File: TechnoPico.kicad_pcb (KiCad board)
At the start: 2 copper layers, 138.3 x 70.6 mm, 160 parts, among them J1 USB_C_Receptacle_USB2.0, J2 Conn_01x02, SW1 Test, SW2 Service, SW3 BOOTSEL, U1 RP2350_60QFN, U2 SN74LV1T34DBV, U3 XC6206PxxxMR, U4 USBLC6-2SC6, Y1 12.000MHz

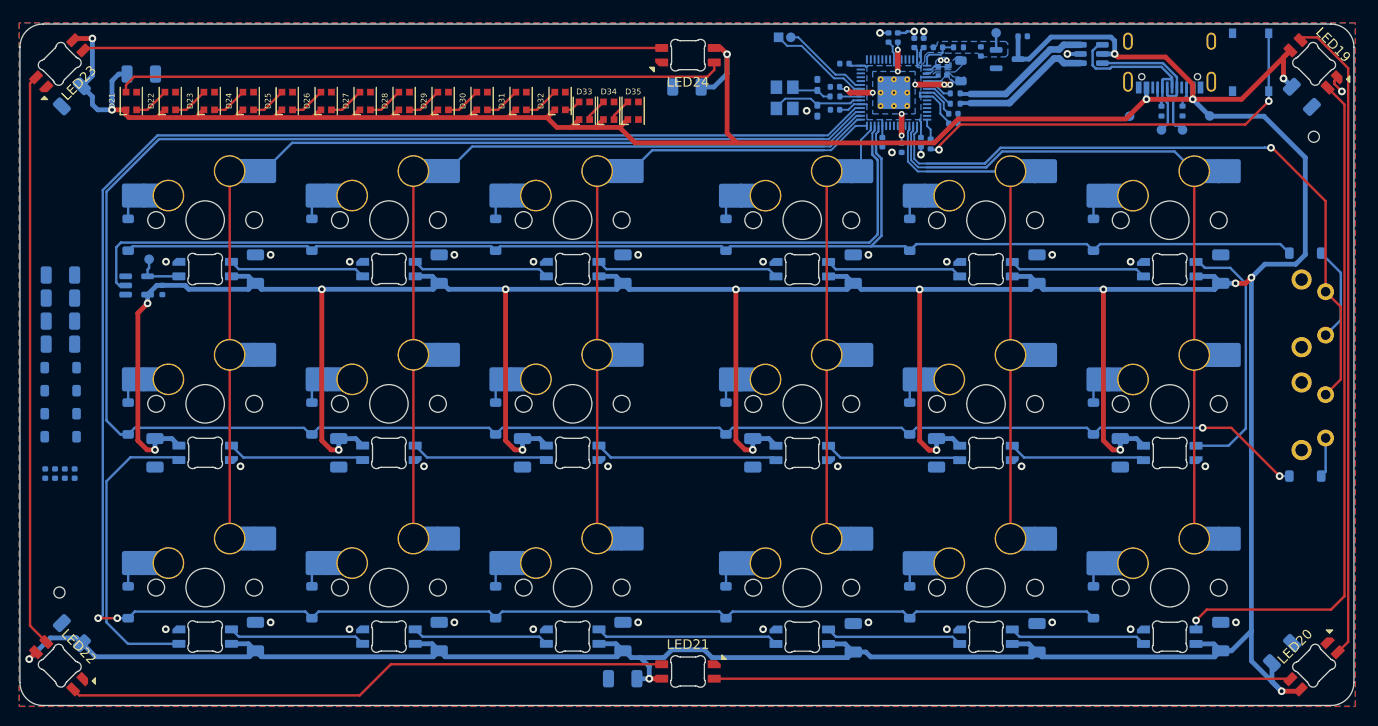
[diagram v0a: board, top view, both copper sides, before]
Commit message: Experimental corner cutouts for mounting
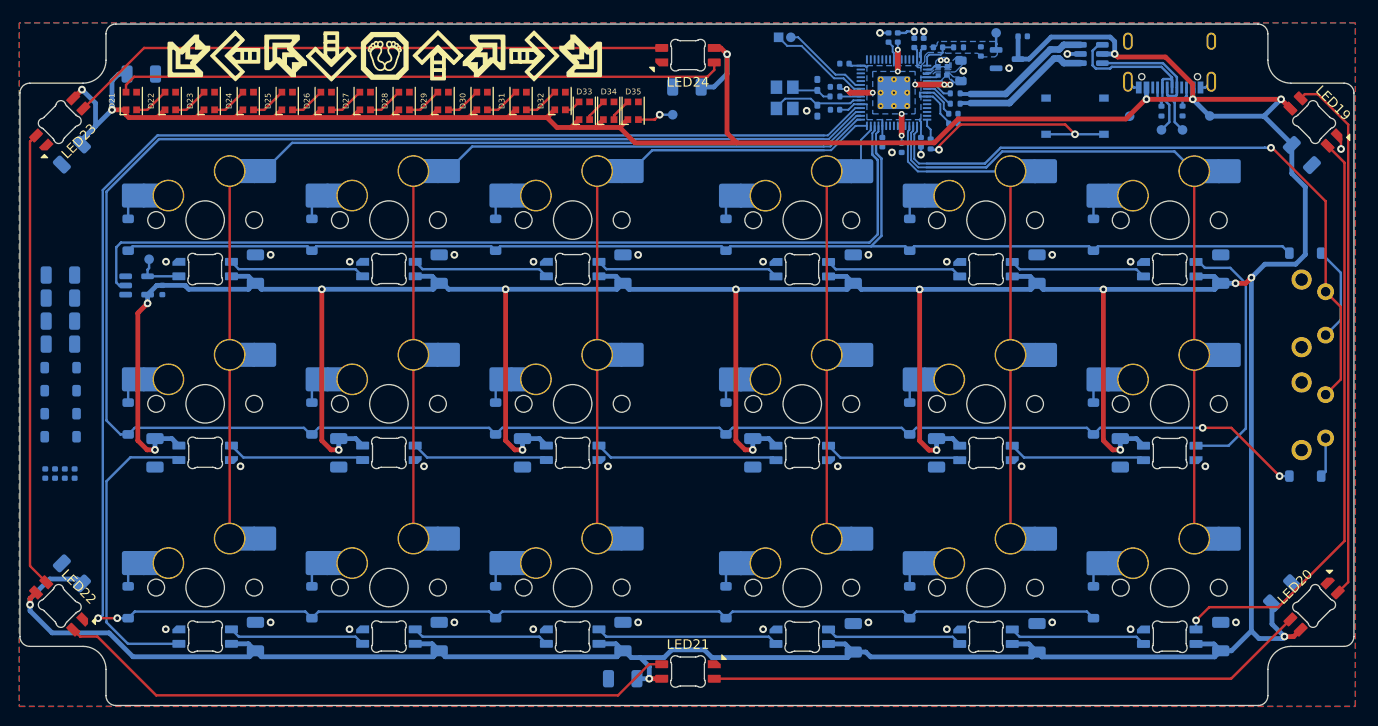
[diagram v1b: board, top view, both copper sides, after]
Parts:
- removed REF** (x2): MountingHole_ToolingHole_1.152mm, MountingHole:MountingHole_ToolingHole_1.152mm
- added TP7: EXT LED, TestPoint:TestPoint_Pad_D1.0mm, B.Cu at (135.2, 60.2)
- moved SW3 19.1 mm to (176.9, 60.4), turned to 0 degrees
- moved C41 6.19 mm to (198.4, 109.8)
- moved LED20 6.19 mm to (201.7, 111.1)
- moved C43 6.19 mm to (72.9, 107.8)
- moved LED22 6.19 mm to (71.7, 111.1)
- moved C40 6.03 mm to (200.4, 64.4)
- moved LED19 6.03 mm to (201.7, 61.0)
- moved C44 6.03 mm to (72.9, 64.3)
- moved LED23 6.03 mm to (71.7, 61.0)
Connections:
- D35 pad 2: unconnected-(D35-DOUT-Pad2) -> LED_EXT
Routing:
- net /BOOTSEL: track 44.4 -> 22.7 mm
- net Net-(LED22-DOUT): track 59.5 -> 47.3 mm
- net Net-(LED19-DOUT): track 67.4 -> 55.4 mm
- net LED_ZONE2: track 70.8 -> 61.4 mm
- net LED_EXT: track 0.00 -> 3.76 mm, vias 0 -> 1
- net Net-(LED21-DOUT): track 62.6 -> 65.2 mm
- net Net-(LED20-DOUT): track 59.8 -> 62.3 mm
- net Net-(LED23-DOUT): track 60.1 -> 62.6 mm
- net GND: track 9.48 -> 11.8 mm, vias 39 -> 41
- net +5V: track 714.0 -> 716.1 mm
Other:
- outline, holes or cut-outs redrawn
- board text added: "DESIGNED BY DJ505 2024"
- board text added: "DOUT"
- board text added: "https://github.com/dj505/TechnoPico"

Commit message: Revert main PCB corner cutouts, add holes to plate
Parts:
- added REF**: MountingHole_ToolingHole_1.152mm, MountingHole:MountingHole_ToolingHole_1.152mm, F.Cu at (71.6, 109.7)
- added REF**: MountingHole_ToolingHole_1.152mm, MountingHole:MountingHole_ToolingHole_1.152mm, F.Cu at (201.7, 62.5)
- moved C41 6.19 mm to (198.4, 116.0)
- moved LED20 6.19 mm to (201.7, 117.3)
- moved C43 6.19 mm to (72.9, 113.9)
- moved LED22 6.19 mm to (71.7, 117.3)
- moved C40 6.03 mm to (200.4, 58.3)
- moved LED19 6.03 mm to (201.7, 54.9)
- moved C44 6.03 mm to (72.9, 58.3)
- moved LED23 6.03 mm to (71.7, 54.9)
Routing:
- net Net-(LED22-DOUT): track 47.3 -> 59.5 mm
- net Net-(LED19-DOUT): track 55.4 -> 67.4 mm
- net LED_ZONE2: track 61.4 -> 70.8 mm
- net Net-(LED21-DOUT): track 65.2 -> 62.6 mm
- net Net-(LED20-DOUT): track 62.3 -> 59.8 mm
- net Net-(LED23-DOUT): track 62.6 -> 60.1 mm
- net +5V: track 716.1 -> 714.0 mm
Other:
- outline, holes or cut-outs redrawn

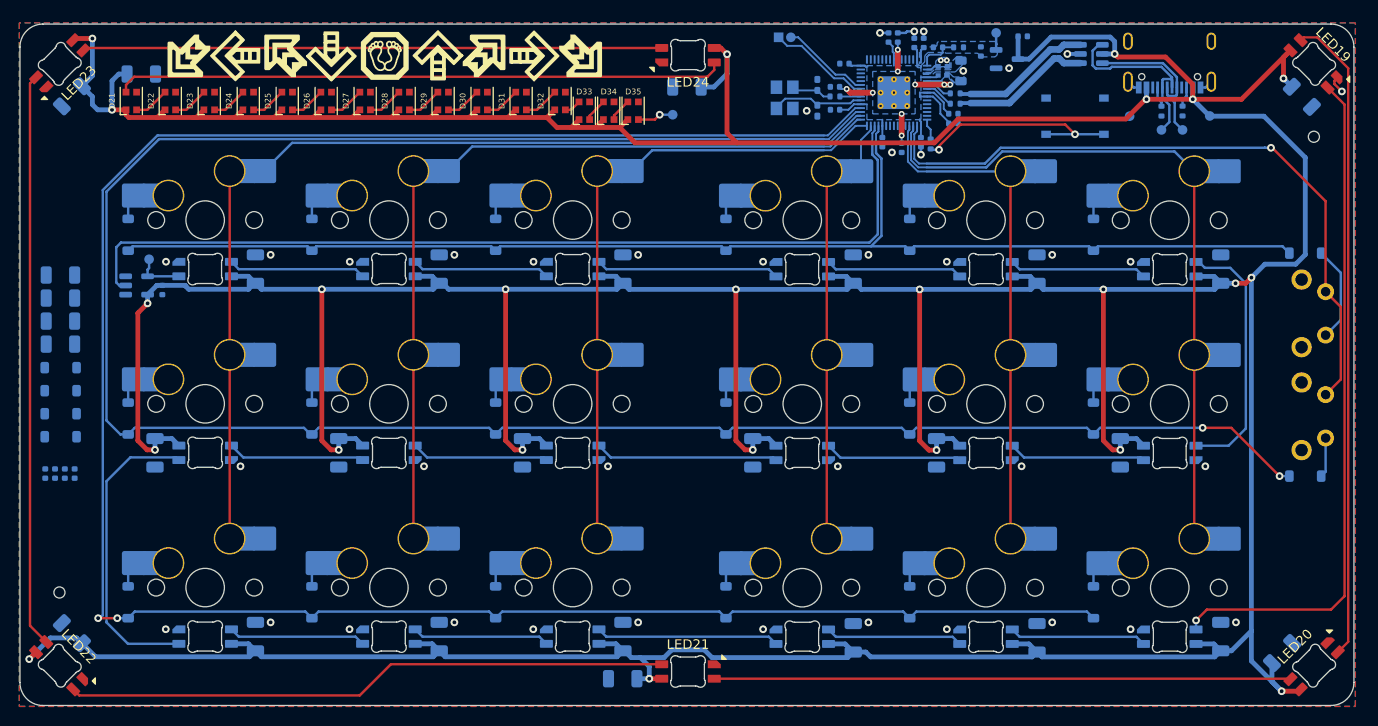
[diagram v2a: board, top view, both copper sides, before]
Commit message: Add flash
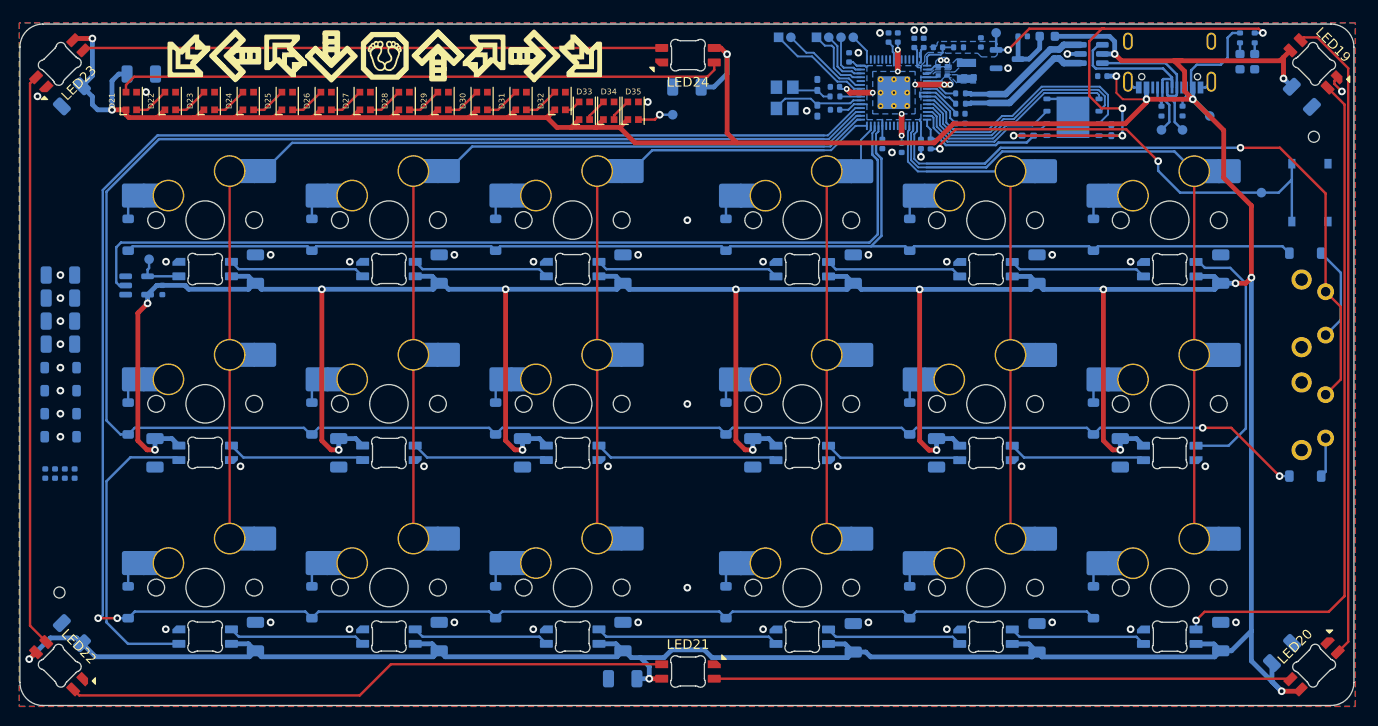
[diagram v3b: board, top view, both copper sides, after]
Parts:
- removed TP2: GND, TestPoint:TestPoint_Pad_D1.0mm
- added C50: 100nF, Capacitor_SMD:C_0402_1005Metric, B.Cu at (179.8, 56.2)
- added C51: 100nF, Capacitor_SMD:C_0402_1005Metric_Pad0.74x0.62mm_HandSolder, B.Cu at (180.7, 61.8)
- added D40: WHITE, LED_SMD:LED_0603_1608Metric, B.Cu at (195.5, 54.7)
- added D41: WHITE, LED_SMD:LED_0603_1608Metric, B.Cu at (194.0, 54.7)
- added F1: 6V 0.5A, Fuse:Fuse_0603_1608Metric, B.Cu at (174.0, 52.1)
- added J3: Conn_01x04, Connector_PinHeader_1.27mm:PinHeader_1x04_P1.27mm_Vertical, B.Cu at (150.1, 52.2)
- added R10: DNF, Resistor_SMD:R_0402_1005Metric_Pad0.72x0.64mm_HandSolder, B.Cu at (172.0, 62.4)
- added R8: 220R, Resistor_SMD:R_0402_1005Metric, B.Cu at (194.0, 52.2)
- added R9: 220R, Resistor_SMD:R_0402_1005Metric, B.Cu at (195.5, 52.2)
- added TP8: BOOTSEL, TestPoint:TestPoint_Pad_D1.0mm, B.Cu at (196.2, 68.3)
- added U5: W25Q32JVZP, Package_SON:WSON-8-1EP_6x5mm_P1.27mm_EP3.4x4.3mm, B.Cu at (176.7, 60.5)
- L1: footprint Inductor_SMD:L_0805_2012Metric -> PA4335.XXXNLT:PA4335.XXXNLT
- moved SW3 25.6 mm to (201.3, 68.3), turned to -90 degrees
- moved C20 0.94 mm to (167.2, 52.7), turned to 90 degrees
- moved C33 0.81 mm to (153.5, 54.3), turned to 90 degrees
- moved C30 0.73 mm to (165.0, 61.1)
- moved C37 0.73 mm to (165.0, 60.1)
- moved L1 0.57 mm to (165.7, 55.7), turned to 0 degrees
- moved R5 0.56 mm to (165.0, 59.1)
- moved R4 0.56 mm to (165.0, 58.0)
- moved C36 0.19 mm to (160.9, 63.2)
- moved C35 0.19 mm to (156.9, 63.2)
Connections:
- net Net-(U1-QSPI_SS) renamed QSPI_SS
- C21 pad 1: +5V -> Net-(U3-VI)
- U1 pad 27: unconnected-(U1-GPIO16-Pad27) -> SPI_RX
- U1 pad 28: unconnected-(U1-GPIO17-Pad28) -> SPI_CS
- U1 pad 29: unconnected-(U1-GPIO18-Pad29) -> SPI_SCK
- U1 pad 31: unconnected-(U1-GPIO19-Pad31) -> SPI_TX
- U1 pad 55: unconnected-(U1-QSPI_SD3-Pad55) -> QSPI_SD3
- U1 pad 56: unconnected-(U1-QSPI_SCLK-Pad56) -> QSPI_SCLK
- U1 pad 57: unconnected-(U1-QSPI_SD0-Pad57) -> QSPI_SD0
- U1 pad 58: unconnected-(U1-QSPI_SD2-Pad58) -> QSPI_SD2
- U1 pad 59: unconnected-(U1-QSPI_SD1-Pad59) -> QSPI_SD1
- U3 pad 3: +5V -> Net-(U3-VI)
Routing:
- net +3V3: track 28.2 -> 88.3 mm, vias 0 -> 5
- net QSPI_SD3: track 0.00 -> 26.1 mm
- net /BOOTSEL: track 22.7 -> 48.4 mm
- net QSPI_SCLK: track 0.00 -> 24.1 mm
- net QSPI_SD0: track 0.00 -> 21.9 mm
- net QSPI_SD2: track 0.00 -> 15.4 mm
- net QSPI_SD1: track 0.00 -> 14.9 mm
- net QSPI_SS: track 2.08 -> 14.8 mm
- net SPI_RX: track 0.00 -> 7.54 mm
- net Net-(U3-VI): track 0.00 -> 6.32 mm
- net SPI_CS: track 0.00 -> 6.11 mm
- net SPI_SCK: track 0.00 -> 5.11 mm
- net SPI_TX: track 0.00 -> 2.89 mm
- net +5V: track 714.0 -> 715.7 mm, vias 24 -> 25
- net Net-(D40-A): track 0.00 -> 1.17 mm
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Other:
- board text added: "3V3 OK"
- board text added: "5V OK"
- board text added: "BOOTSEL"
- board text added: "CK"
- board text added: "CS"
- board text added: "RX"
- board text added: "SPI"
- board text added: "SWD"
- board text added: "TX"
- board text removed: "GND"

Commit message: Reroute 5V to LEDs to split up the ground plane less, etc
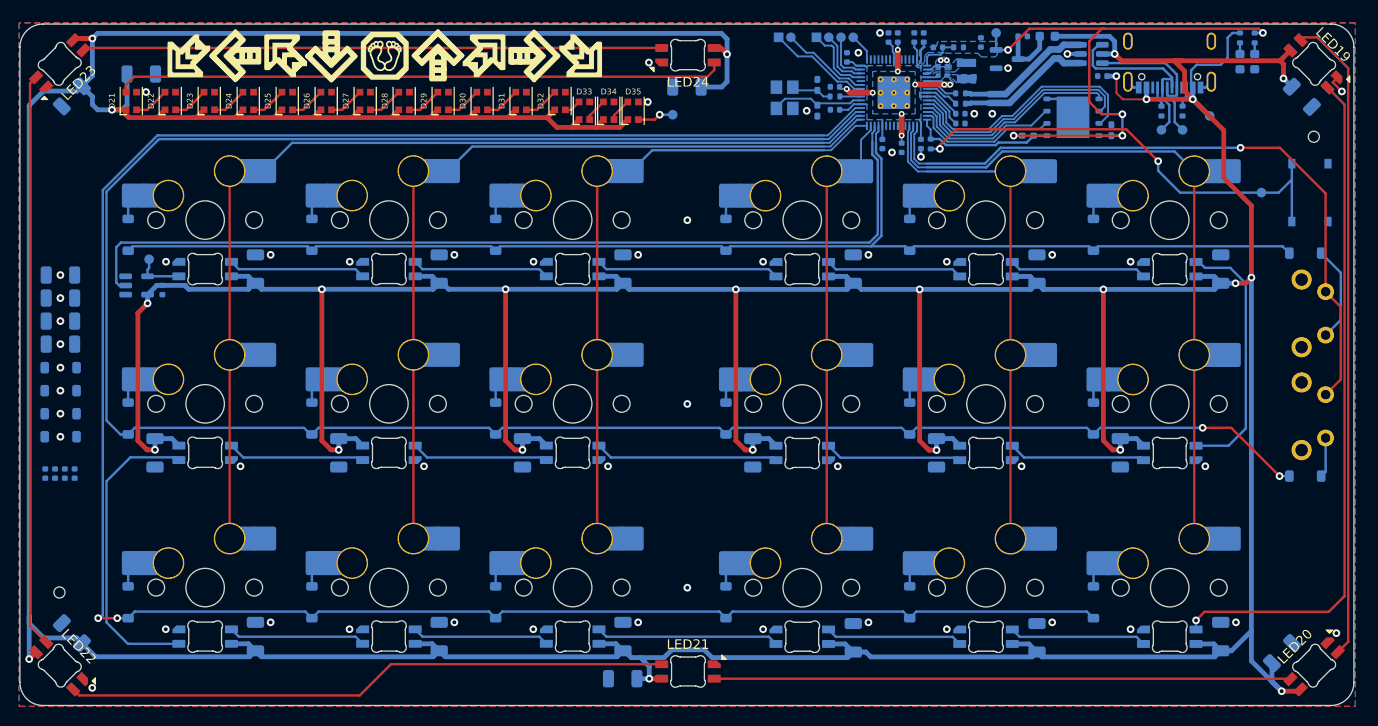
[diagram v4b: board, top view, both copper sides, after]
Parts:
- moved C31 0.56 mm to (161.2, 52.2)
- moved C38 0.56 mm to (160.3, 52.2)
- moved C33 0.22 mm to (153.3, 54.3)
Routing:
- net +5V: track 715.7 -> 781.1 mm
- net +3V3: track 88.3 -> 89.8 mm
- net GND: track 12.8 -> 12.9 mm, vias 55 -> 57
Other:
- board text added: "DESIGNED BY DJ505 2025"
- board text removed: "DESIGNED BY DJ505 2024"

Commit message: Finishing touches
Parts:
- C22, C23, C51: footprint Capacitor_SMD:C_0402_1005Metric_Pad0.74x0.62mm_HandSolder -> Capacitor_SMD:C_0402_1005Metric
- moved C51 0.09 mm to (180.7, 61.9)
